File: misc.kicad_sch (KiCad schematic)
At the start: 107 parts, among them CN2 Expansion, CN3 Cartridge, CN5 1P, CN504 AV Out, CN6 2P, CN7 Barrel_Jack, IC601 74ACT241, IC701 PIC16F630/18324, IC801 TPS564257DRLR, IC951 THS7374, J2 EXT, Q801 MMBT3904

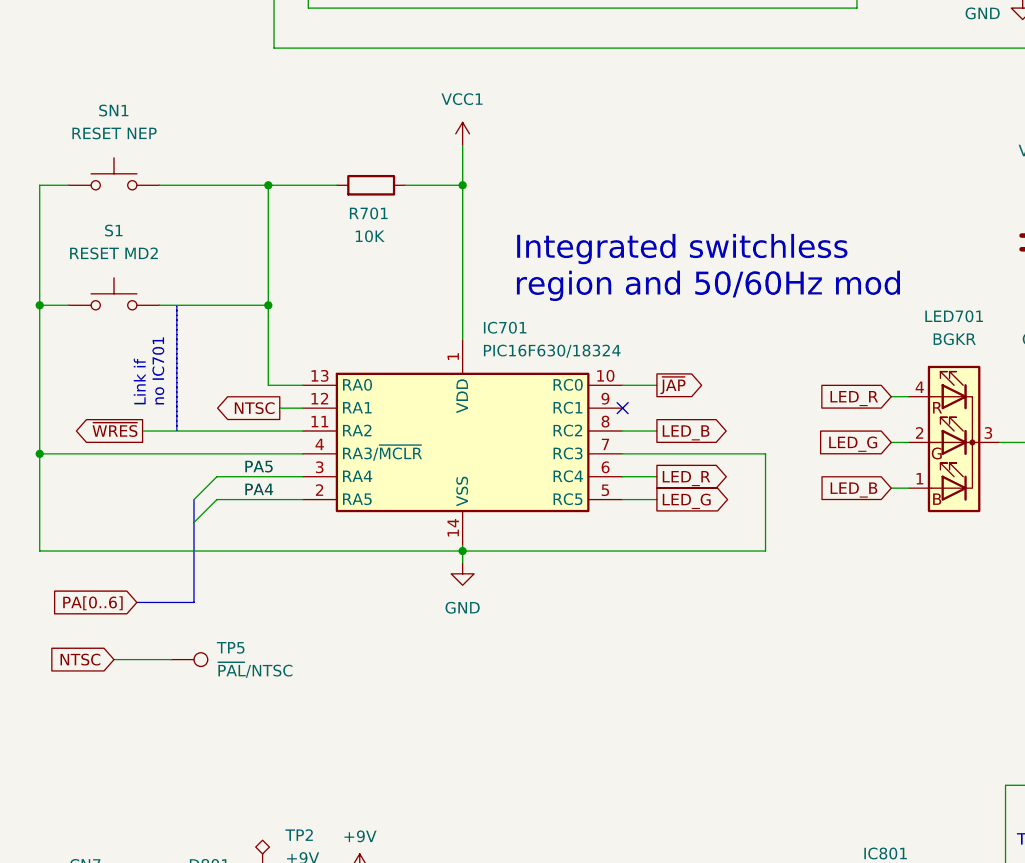
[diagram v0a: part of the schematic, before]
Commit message: Add resistors for IGR, including PA6/SELECT line.
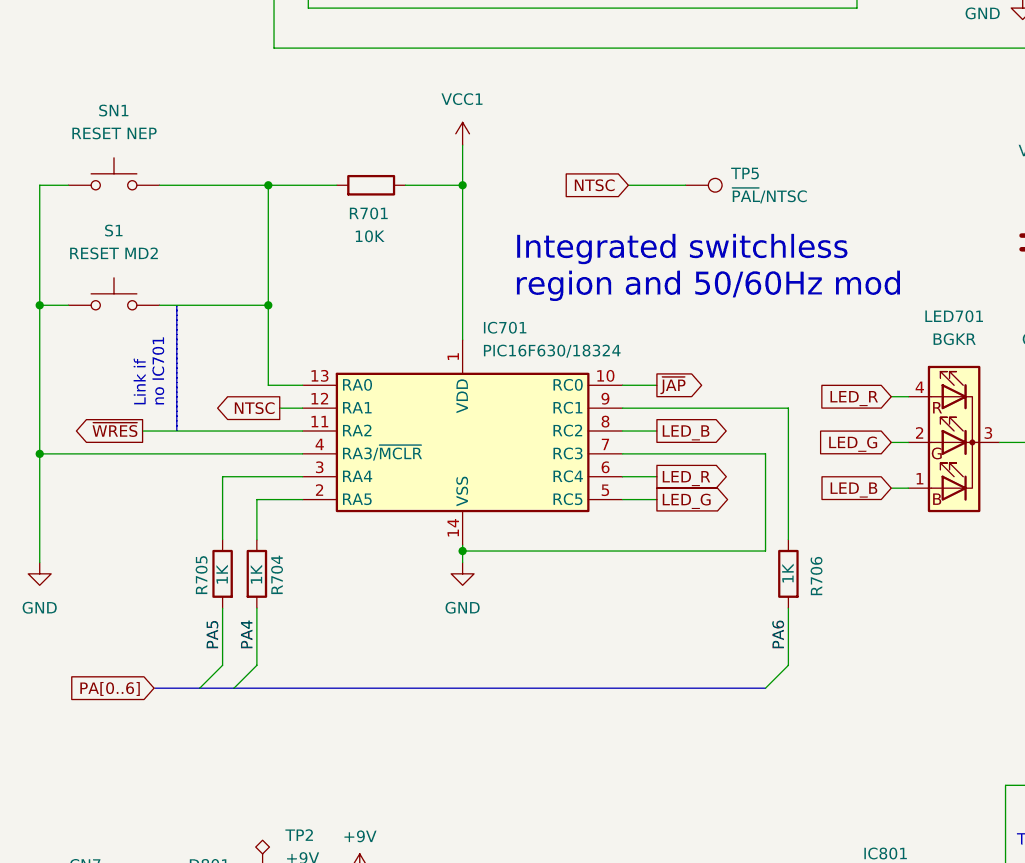
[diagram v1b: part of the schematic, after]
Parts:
- added R704, R705, R706: 1K, Resistor_SMD:R_0805_2012Metric, symbol Device:R
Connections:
- net PA4: now also R704.2; no longer IC701.2 (RA5)
- net PA5: now also R705.2; no longer IC701.3 (RA4)
- net PA6: now also R706.2
- net at IC701.9 (RC1): now also R706.1
- new net: IC701.2 (RA5), R704.1
- new net: IC701.3 (RA4), R705.1
- no-connect marks 8 -> 7
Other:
- moved on the sheet: TP5

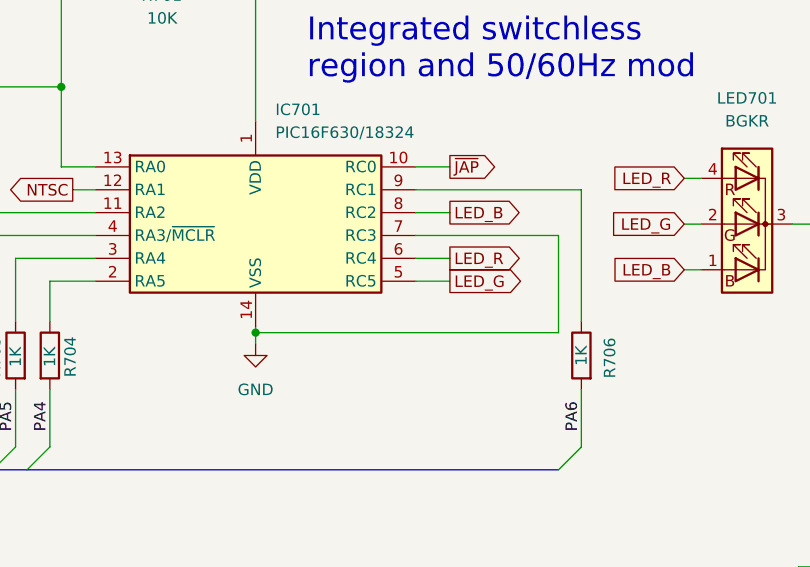
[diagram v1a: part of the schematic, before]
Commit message: Route /M3 to PIC in case useful for IGR or other functionality. Remove solder mask around edge connector fingers.
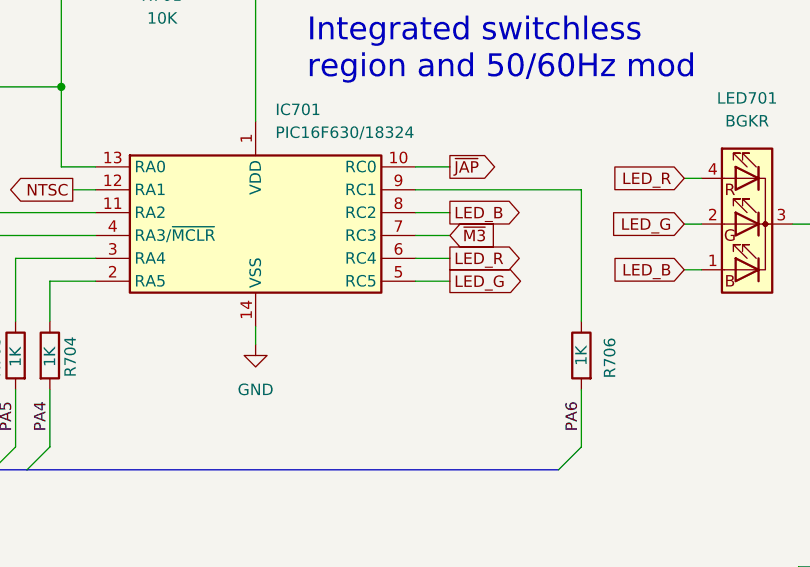
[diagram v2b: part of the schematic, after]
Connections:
- net GND: no longer IC701.7 (RC3)
- net ~{M3}: now also IC701.7 (RC3)
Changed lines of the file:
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@@
 	)
 	(junction
-		(at 66.675 179.705)
-		(diameter 0)
-		(color 0 0 0 0)
-	)
-	(junction
 		(at 305.435 90.17)
 		(diameter 0)
@@
 	(wire
 		(pts
-			(xy 84.455 168.91) (xy 100.33 168.91)
+			(xy 84.455 168.91) (xy 88.265 168.91)
 		)
 		(stroke
@@
 	(wire
 		(pts
-			(xy 66.675 179.705) (xy 100.33 179.705)
-		)
-		(stroke
-			(width 0)
-			(type default)
-		)
-	)
-	(wire
-		(pts
 			(xy 22.225 53.975) (xy 31.75 53.975)
 		)
@@
 	(wire
 		(pts
-			(xy 100.33 179.705) (xy 100.33 168.91)
-		)
-		(stroke
-			(width 0)
-			(type default)
-		)
-	)
-	(wire
-		(pts
 			(xy 44.45 231.775) (xy 44.45 247.015)
 		)
@@
 	(wire
 		(pts
-			(xy 66.675 179.07) (xy 66.675 179.705)
+			(xy 66.675 179.07) (xy 66.675 180.975)
 		)
 		(stroke
@@
 	(wire
 		(pts
-			(xy 66.675 179.705) (xy 66.675 180.975)
-		)
-		(stroke
-			(width 0)
-			(type default)
-		)
-	)
-	(wire
-		(pts
 			(xy 239.395 210.82) (xy 247.65 210.82)
 		)
@@
 				(hide yes)
 			)
+		)
+	)
+	(global_label "~{M3}"
+		(shape input)
+		(at 88.265 168.91 0)
+		(fields_autoplaced yes)
+		(effects
+			(font
+				(size 1.27 1.27)
+			)
+			(justify left)
+		)
+		(property "Intersheetrefs" "${INTERSHEET_REFS}"
+			(at 93.9111 168.91 0)
+			(effects
+				(font
+					(size 1.27 1.27)
+				)
+				(justify left)
+				(hide yes)
+			)
